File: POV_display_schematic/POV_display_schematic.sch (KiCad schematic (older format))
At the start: 146 parts, among them J1 USB_B_Micro, J3 HC05/06 Port, J4 6PinDebugPort, Q2 MMBT3904, Q3 MMBT3906, SW1 RST, SW2 BOOT, U1 HT7325, U10 74HC595, U11 74HC595, U2 TP4056, U3 74HC595, U4 74HC595, U5 74HC595, U6 74HC595, U7 74HC595, U8 74HC595, U9 STM32L051C8Tx, Y1 32.768 KHz

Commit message: Minor schematic changes
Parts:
- removed R13, R14, R15, R16, R17, R18, R20, R21, R22, R23, R24, R25, R27, R28, R29, R30, R31, R32, R33, R34, R35, R36, R37, R38, R39, R40, R41, R42, R43, R44, R45, R46, R47, R48, R49, R50, R51, R52, R53, R54, R55, R56, R57, R58, R59, R60, R61, R62, R63, R64, R65, R66, R67, R68, R69, R70, R71, R72, R73, R74: 10K, Resistor_SMD:R_0603_1608Metric, symbol Device:R
- added R? (x20): 470R, Resistor_SMD:R_0603_1608Metric, symbol Device:R
- added R? (x40): 1K, Resistor_SMD:R_0603_1608Metric, symbol Device:R
- R12: value 10K -> 470R
- R19, R26: value 10K -> 1K
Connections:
- net led_0_B: now also R12.1, U4.6 (QG); no longer R26.1, U4.15 (QA)
- net led_0_G: now also R26.1, U4.15 (QA); no longer R19.1, U4.7 (QH)
- net led_0_R: now also R19.1, U4.7 (QH); no longer R12.1, U4.6 (QG)
- net led_10_B: now also U3.15 (QA), R?.1; no longer U10.2 (QC)
- net led_10_G: now also U10.2 (QC), R?.1; no longer U10.1 (QB)
- net led_10_R: now also U10.1 (QB), R?.1; no longer U3.15 (QA)
- net led_11_B: now also U3.5 (QF), R?.1; no longer U3.7 (QH)
- net led_11_G: now also U3.7 (QH), R?.1; no longer U3.6 (QG)
- net led_11_R: now also U3.6 (QG), R?.1; no longer U3.5 (QF)
- net led_12_B: now also U3.2 (QC), R?.1; no longer U3.4 (QE)
- net led_12_G: now also U3.4 (QE), R?.1; no longer U3.3 (QD)
- net led_12_R: now also U3.3 (QD), R?.1; no longer U3.2 (QC)
- net led_13_B: now also U6.7 (QH), R?.1; no longer U3.1 (QB)
- net led_13_G: now also U3.1 (QB), R?.1; no longer U6.15 (QA)
- net led_13_R: now also U6.15 (QA), R?.1; no longer U6.7 (QH)
- net led_14_B: now also U6.4 (QE), R?.1; no longer U6.6 (QG)
- net led_14_G: now also U6.6 (QG), R?.1; no longer U6.5 (QF)
- net led_14_R: now also U6.5 (QF), R?.1; no longer U6.4 (QE)
- net led_15_B: now also U6.1 (QB), R?.1; no longer U6.3 (QD)
- net led_15_G: now also U6.3 (QD), R?.1; no longer U6.2 (QC)
- net led_15_R: now also U6.2 (QC), R?.1; no longer U6.1 (QB)
- net led_16_B: now also U8.6 (QG), R?.1; no longer U8.15 (QA)
- net led_16_G: now also U8.15 (QA), R?.1; no longer U8.7 (QH)
- net led_16_R: now also U8.7 (QH), R?.1; no longer U8.6 (QG)
- net led_17_B: now also U8.3 (QD), R?.1; no longer U8.5 (QF)
- net led_17_G: now also U8.5 (QF), R?.1; no longer U8.4 (QE)
- net led_17_R: now also U8.4 (QE), R?.1; no longer U8.3 (QD)
- net led_18_B: now also U11.15 (QA), R?.1; no longer U8.2 (QC)
- net led_18_G: now also U8.2 (QC), R?.1; no longer U8.1 (QB)
- net led_18_R: now also U8.1 (QB), R?.1; no longer U11.15 (QA)
- net led_19_B: now also U11.5 (QF), R?.1; no longer U11.7 (QH)
- net led_19_G: now also U11.7 (QH), R?.1; no longer U11.6 (QG)
- net led_19_R: now also U11.6 (QG), R?.1; no longer U11.5 (QF)
- net led_1_B: now also U4.3 (QD), R?.1; no longer U4.5 (QF)
- net led_1_G: now also U4.5 (QF), R?.1; no longer U4.4 (QE)
- net led_1_R: now also U4.4 (QE), R?.1; no longer U4.3 (QD)
- net led_20_B: now also U11.2 (QC), R?.1; no longer U11.4 (QE)
- net led_20_G: now also U11.4 (QE), R?.1; no longer U11.3 (QD)
- net led_20_R: now also U11.3 (QD), R?.1; no longer U11.2 (QC)
- net led_2_B: now also U5.15 (QA), R?.1; no longer U4.2 (QC)
- net led_2_G: now also U4.2 (QC), R?.1; no longer U4.1 (QB)
- net led_2_R: now also U4.1 (QB), R?.1; no longer U5.15 (QA)
- net led_3_B: now also U5.5 (QF), R?.1; no longer U5.7 (QH)
- net led_3_G: now also U5.7 (QH), R?.1; no longer U5.6 (QG)
- net led_3_R: now also U5.6 (QG), R?.1; no longer U5.5 (QF)
- net led_4_B: now also U5.2 (QC), R?.1; no longer U5.4 (QE)
- net led_4_G: now also U5.4 (QE), R?.1; no longer U5.3 (QD)
- net led_4_R: now also U5.3 (QD), R?.1; no longer U5.2 (QC)
- net led_5_B: now also U7.7 (QH), R?.1; no longer U5.1 (QB)
- net led_5_G: now also U5.1 (QB), R?.1; no longer U7.15 (QA)
- net led_5_R: now also U7.15 (QA), R?.1; no longer U7.7 (QH)
- net led_6_B: now also U7.4 (QE), R?.1; no longer U7.6 (QG)
- net led_6_G: now also U7.6 (QG), R?.1; no longer U7.5 (QF)
- net led_6_R: now also U7.5 (QF), R?.1; no longer U7.4 (QE)
- net led_7_B: now also U7.1 (QB), R?.1; no longer U7.3 (QD)
- net led_7_G: now also U7.3 (QD), R?.1; no longer U7.2 (QC)
- net led_7_R: now also U7.2 (QC), R?.1; no longer U7.1 (QB)
- net led_8_B: now also U10.6 (QG), R?.1; no longer U10.15 (QA)
- net led_8_G: now also U10.15 (QA), R?.1; no longer U10.7 (QH)
- net led_8_R: now also U10.7 (QH), R?.1; no longer U10.6 (QG)
- net led_9_B: now also U10.3 (QD), R?.1; no longer U10.5 (QF)
- net led_9_G: now also U10.5 (QF), R?.1; no longer U10.4 (QE)
- net led_9_R: now also U10.4 (QE), R?.1; no longer U10.3 (QD)
- net at D4.3 (BA): now also R?.2
- net at D4.2 (GA): now also R?.2
- net at D4.1 (RA): now also R?.2
- net at D5.3 (BA): now also R?.2
- net at D5.2 (GA): now also R?.2
- net at D5.1 (RA): now also R?.2
- net at D6.3 (BA): now also R?.2
- net at D6.2 (GA): now also R?.2
- net at D6.1 (RA): now also R?.2
- net at D7.3 (BA): now also R?.2
- net at D7.2 (GA): now also R?.2
- net at D7.1 (RA): now also R?.2
- net at D8.3 (BA): now also R?.2
- net at D8.2 (GA): now also R?.2
- net at D8.1 (RA): now also R?.2
- net at D9.3 (BA): now also R?.2
- net at D9.2 (GA): now also R?.2
- net at D9.1 (RA): now also R?.2
- net at D10.3 (BA): now also R?.2
- net at D10.2 (GA): now also R?.2
- net at D10.1 (RA): now also R?.2
- net at D11.3 (BA): now also R?.2
- net at D11.2 (GA): now also R?.2
- net at D11.1 (RA): now also R?.2
- net at D12.3 (BA): now also R?.2
- net at D12.2 (GA): now also R?.2
- net at D12.1 (RA): now also R?.2
- net at D13.3 (BA): now also R?.2
- net at D13.2 (GA): now also R?.2
- net at D13.1 (RA): now also R?.2
- net at D14.3 (BA): now also R?.2
- net at D14.2 (GA): now also R?.2
- net at D14.1 (RA): now also R?.2
- net at D15.3 (BA): now also R?.2
- net at D15.2 (GA): now also R?.2
- net at D15.1 (RA): now also R?.2
- net at D16.3 (BA): now also R?.2
- net at D16.2 (GA): now also R?.2
- net at D16.1 (RA): now also R?.2
- net at D17.3 (BA): now also R?.2
- net at D17.2 (GA): now also R?.2
- net at D17.1 (RA): now also R?.2
- net at D18.3 (BA): now also R?.2
- net at D18.2 (GA): now also R?.2
- net at D18.1 (RA): now also R?.2
- net at D19.3 (BA): now also R?.2
- net at D19.2 (GA): now also R?.2
- net at D19.1 (RA): now also R?.2
- net at D20.3 (BA): now also R?.2
- net at D20.2 (GA): now also R?.2
- net at D20.1 (RA): now also R?.2
- net at D21.3 (BA): now also R?.2
- net at D21.2 (GA): now also R?.2
- net at D21.1 (RA): now also R?.2
- net at D22.3 (BA): now also R?.2
- net at D22.2 (GA): now also R?.2
- net at D22.1 (RA): now also R?.2
- net at D23.3 (BA): now also R?.2
- net at D23.2 (GA): now also R?.2
- net at D23.1 (RA): now also R?.2

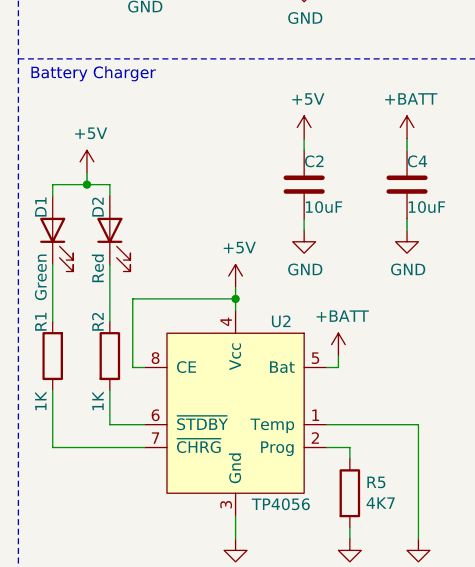
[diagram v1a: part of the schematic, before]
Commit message: Recorded results and updated README
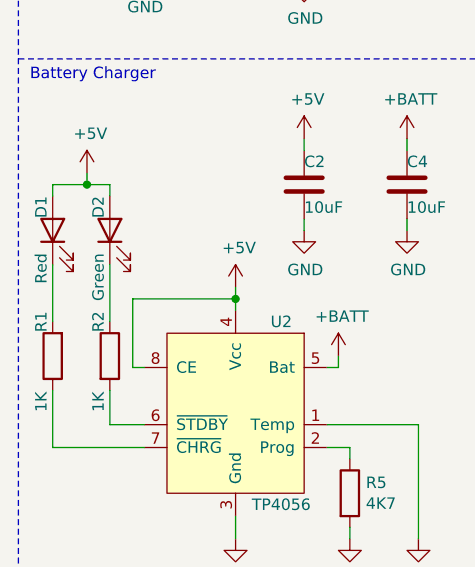
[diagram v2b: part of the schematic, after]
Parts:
- D1: value Green -> Red
- D2: value Red -> Green
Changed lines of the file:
@@
 	-1   0    0    1
-$EndComp
-$Comp
-L Device:LED D2
-U 1 1 63709874
-P 900 4200
-F 0 "D2" H 1050 4250 50  0000 R CNN
-F 1 "Red" H 800 4250 50  0000 R CNN
-F 2 "LED_SMD:LED_0805_2012Metric_Pad1.15x1.40mm_HandSolder" H 900 4200 50  0001 C CNN
-F 3 "~" H 900 4200 50  0001 C CNN
-	1    900  4200
-	0    -1   -1   0
-$EndComp
-$Comp
-L Device:LED D1
-U 1 1 6370B345
-P 650 4200
-F 0 "D1" H 800 4250 50  0000 R CNN
-F 1 "Green" H 550 4250 50  0000 R CNN
-F 2 "LED_SMD:LED_0805_2012Metric_Pad1.15x1.40mm_HandSolder" H 650 4200 50  0001 C CNN
-F 3 "~" H 650 4200 50  0001 C CNN
-	1    650  4200
-	0    -1   -1   0
 $EndComp
 Wire Wire Line
@@
 Text Label 11650 2150 0    50   ~ 0
 led_1_R
+$Comp
+L Device:LED D1
+U 1 1 6370B345
+P 650 4200
+F 0 "D1" H 800 4250 50  0000 R CNN
+F 1 "Red" H 550 4250 50  0000 R CNN
+F 2 "LED_SMD:LED_0805_2012Metric_Pad1.15x1.40mm_HandSolder" H 650 4200 50  0001 C CNN
+F 3 "~" H 650 4200 50  0001 C CNN
+	1    650  4200
+	0    -1   -1   0
+$EndComp
+$Comp
+L Device:LED D2
+U 1 1 63709874
+P 900 4200
+F 0 "D2" H 1050 4250 50  0000 R CNN
+F 1 "Green" H 800 4250 50  0000 R CNN
+F 2 "LED_SMD:LED_0805_2012Metric_Pad1.15x1.40mm_HandSolder" H 900 4200 50  0001 C CNN
+F 3 "~" H 900 4200 50  0001 C CNN
+	1    900  4200
+	0    -1   -1   0
+$EndComp
 $EndSCHEMATC
